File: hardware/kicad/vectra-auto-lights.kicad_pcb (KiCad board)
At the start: 2 copper layers, 120 x 80 mm, 51 parts

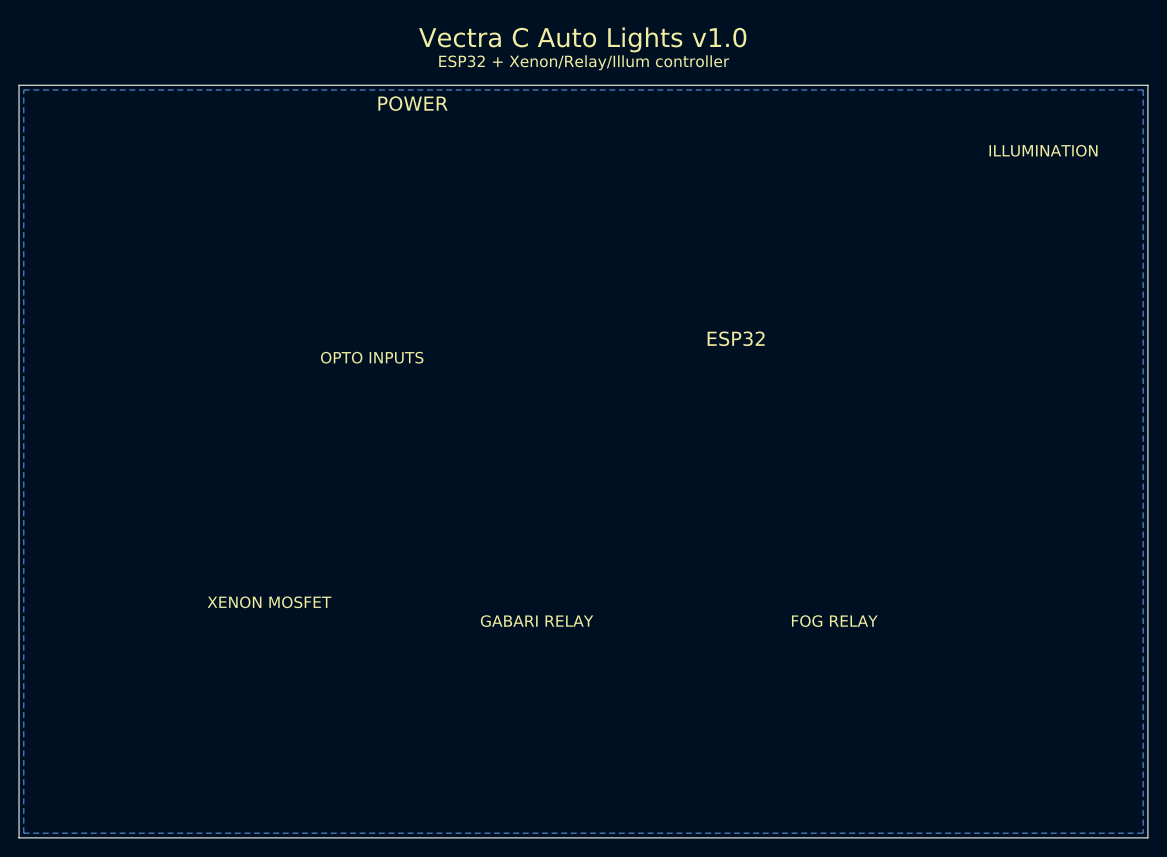
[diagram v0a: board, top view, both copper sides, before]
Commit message: Fix KiCad 10 compatibility: remove invalid syntax, fix library names
PCB (.kicad_pcb):
- Remove all ;; comments (not valid in S-expression format)
- Replace incomplete footprint stubs with proper mounting hole pads
- Keep board outline 120x80mm + GND pour; components added via
  Tools -> Update PCB from Schematic

Schematic (.kicad_sch):
- Opto:PC817 -> Isolator:PC817 (library renamed in KiCad 8+)
- Relay:G5V-2 (DPDT) -> Relay:G5V-1 (SPDT, correct for K1/K2)
- Regenerate vectra-auto-lights.kicad_sch

Co-Authored-By: Claude Sonnet 4.6 <noreply@anthropic.com>
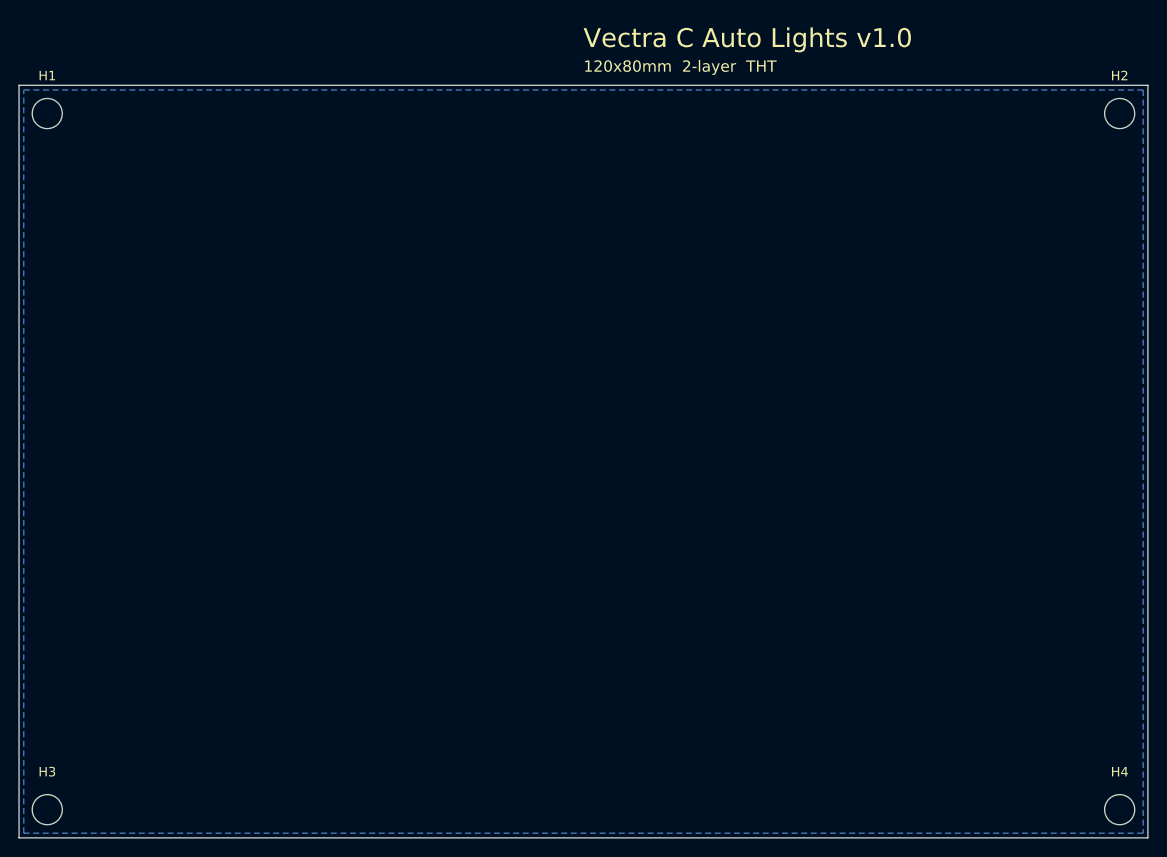
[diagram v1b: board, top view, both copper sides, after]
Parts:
- removed ?: , Connector_JST:JST_XH_B3B-XH-A_1x03_P2.50mm_Vertical
- removed ? (x3): , Diode_THT:D_DO-201AD_P12.70mm_Horizontal
- removed ? (x2): , Package_TO_SOT_THT:TO-220-3_Vertical
- removed ?: , Capacitor_THT:CP_Radial_D8.0mm_P3.50mm
- removed ?: , Capacitor_THT:C_Disc_D5.0mm_W2.5mm_P2.50mm
- removed ? (x13): , Resistor_THT:R_Axial_DIN0207_L6.3mm_D2.5mm_P10.16mm_Horizontal
- removed ? (x3): , Package_DIP:DIP-4_W7.62mm
- removed ?: , Connector_JST:JST_XH_B4B-XH-A_1x04_P2.50mm_Vertical
- removed ?: , RF_Module:ESP32-WROOM-32
- removed ? (x4): , Package_TO_SOT_THT:TO-92_Inline
- removed ? (x2): , Connector_JST:JST_XH_B5B-XH-A_1x05_P2.50mm_Vertical
- removed ? (x2): , Relay_THT:Relay_SPDT_SANYOU_SRD_Series_RM5
- removed ? (x9): , Diode_THT:D_DO-41_SOD81_P10.16mm_Horizontal
- removed ? (x4): , MountingHole:MountingHole_3.2mm_M3
- removed ?: , Connector_JST:JST_XH_B2B-XH-A_1x02_P2.50mm_Vertical
- removed ? (x3): , Fuse:Fuseholder_Cylinder_5x20mm_Schurter_0031_8201_Horizontal_Open
- added H1: M3, MountingHole:MountingHole_3.2mm_M3, F.Cu at (3.00, 3.00)
- added H2: M3, MountingHole:MountingHole_3.2mm_M3, F.Cu at (117.0, 3.00)
- added H3: M3, MountingHole:MountingHole_3.2mm_M3, F.Cu at (3.00, 77.0)
- added H4: M3, MountingHole:MountingHole_3.2mm_M3, F.Cu at (117.0, 77.0)
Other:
- board text added: "120x80mm 2-layer THT"
- board text removed: "ESP32"
- board text removed: "ESP32 + Xenon/Relay/Illum controller"
- board text removed: "FOG RELAY"
- board text removed: "GABARI RELAY"
- board text removed: "ILLUMINATION"
- board text removed: "OPTO INPUTS"
- board text removed: "POWER"
- board text removed: "XENON MOSFET"

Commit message: docs: пълен pinout.md на български + обновени KiCad файлове
- docs/pinout.md: преведен изцяло на чист български, добавена бърза
  справочна таблица с всички 9 сигнала (местоположение, пин, бушон,
  условие) — базирано на Ръководство 209, Глава 12 + схеми стр. 328-335
- hardware/kicad/vectra-auto-lights.kicad_sch: обновена схема
- hardware/kicad/vectra-auto-lights.kicad_pcb: обновен PCB layout
- .gitignore: добавени KiCad autosave, backup и .kicad_prl файлове

Co-Authored-By: Claude Sonnet 4.6 <noreply@anthropic.com>
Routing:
- added copper zone on B.Cu, net (none)
- removed copper zone on B.Cu, net GND
